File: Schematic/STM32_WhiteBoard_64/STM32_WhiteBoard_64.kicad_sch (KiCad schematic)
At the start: 59 parts, among them J1 SWDIO+Serial, J2 USB_B_Micro, J3 Header2, J4 Header1, Q1 BC847BS, Q1 Si3493DDV, Q2 BC857BS, SW1 Boot0, SW2 Reset, SW3 User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

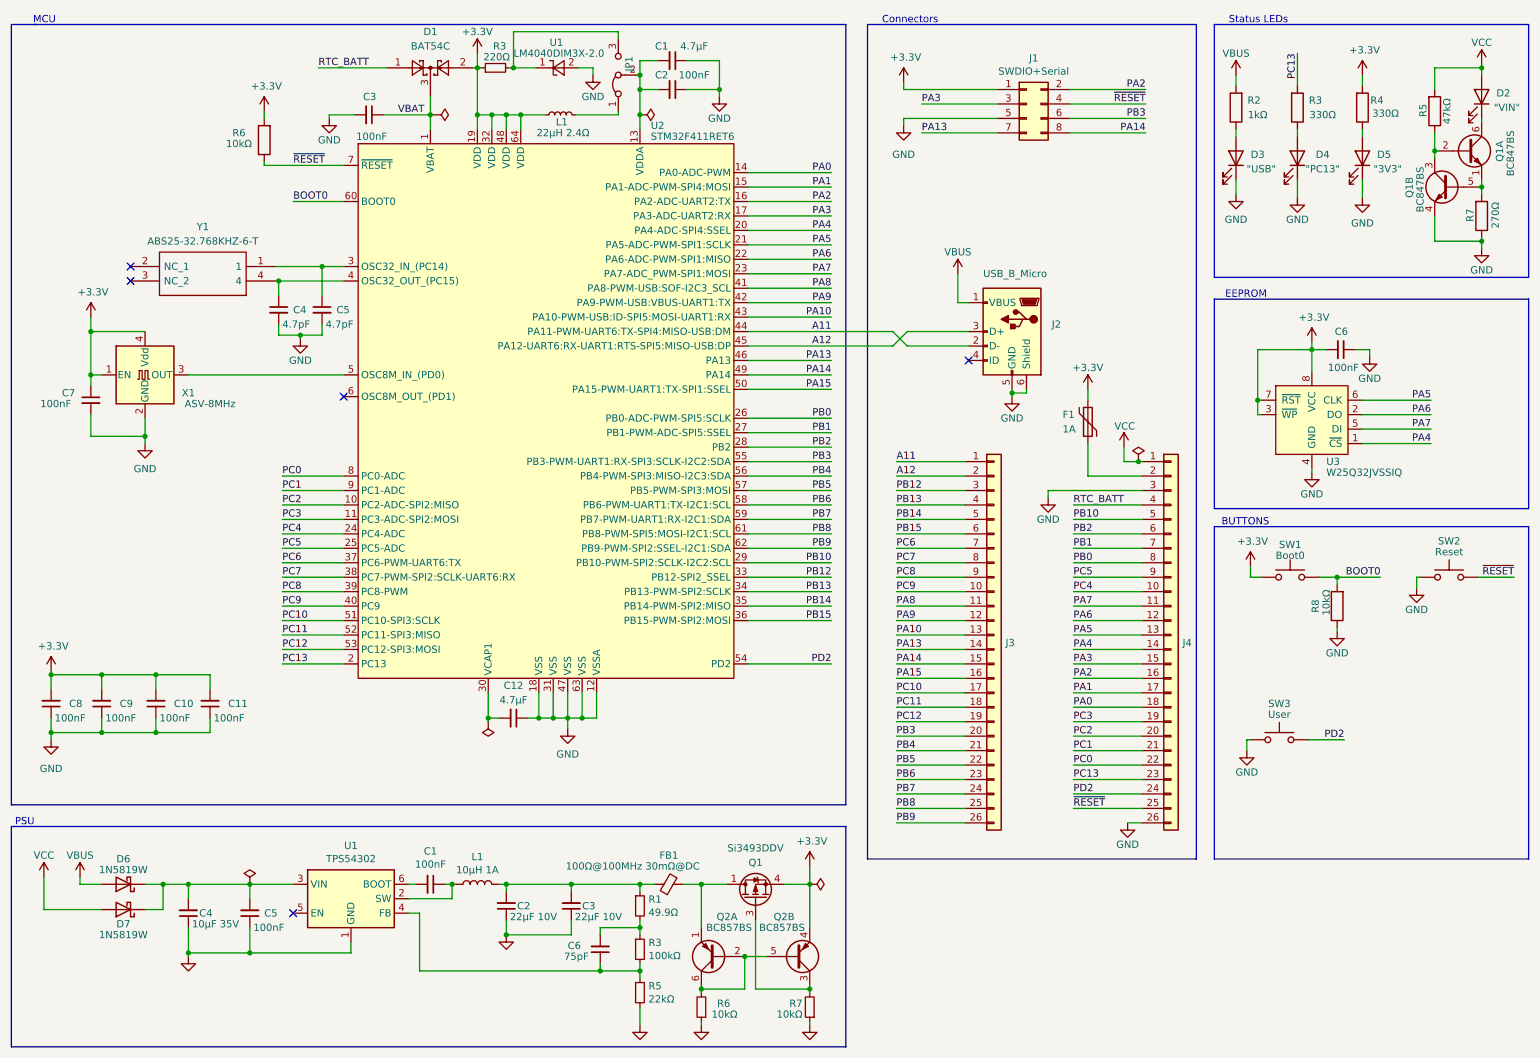
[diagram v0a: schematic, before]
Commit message: Added ESD protection for USB.
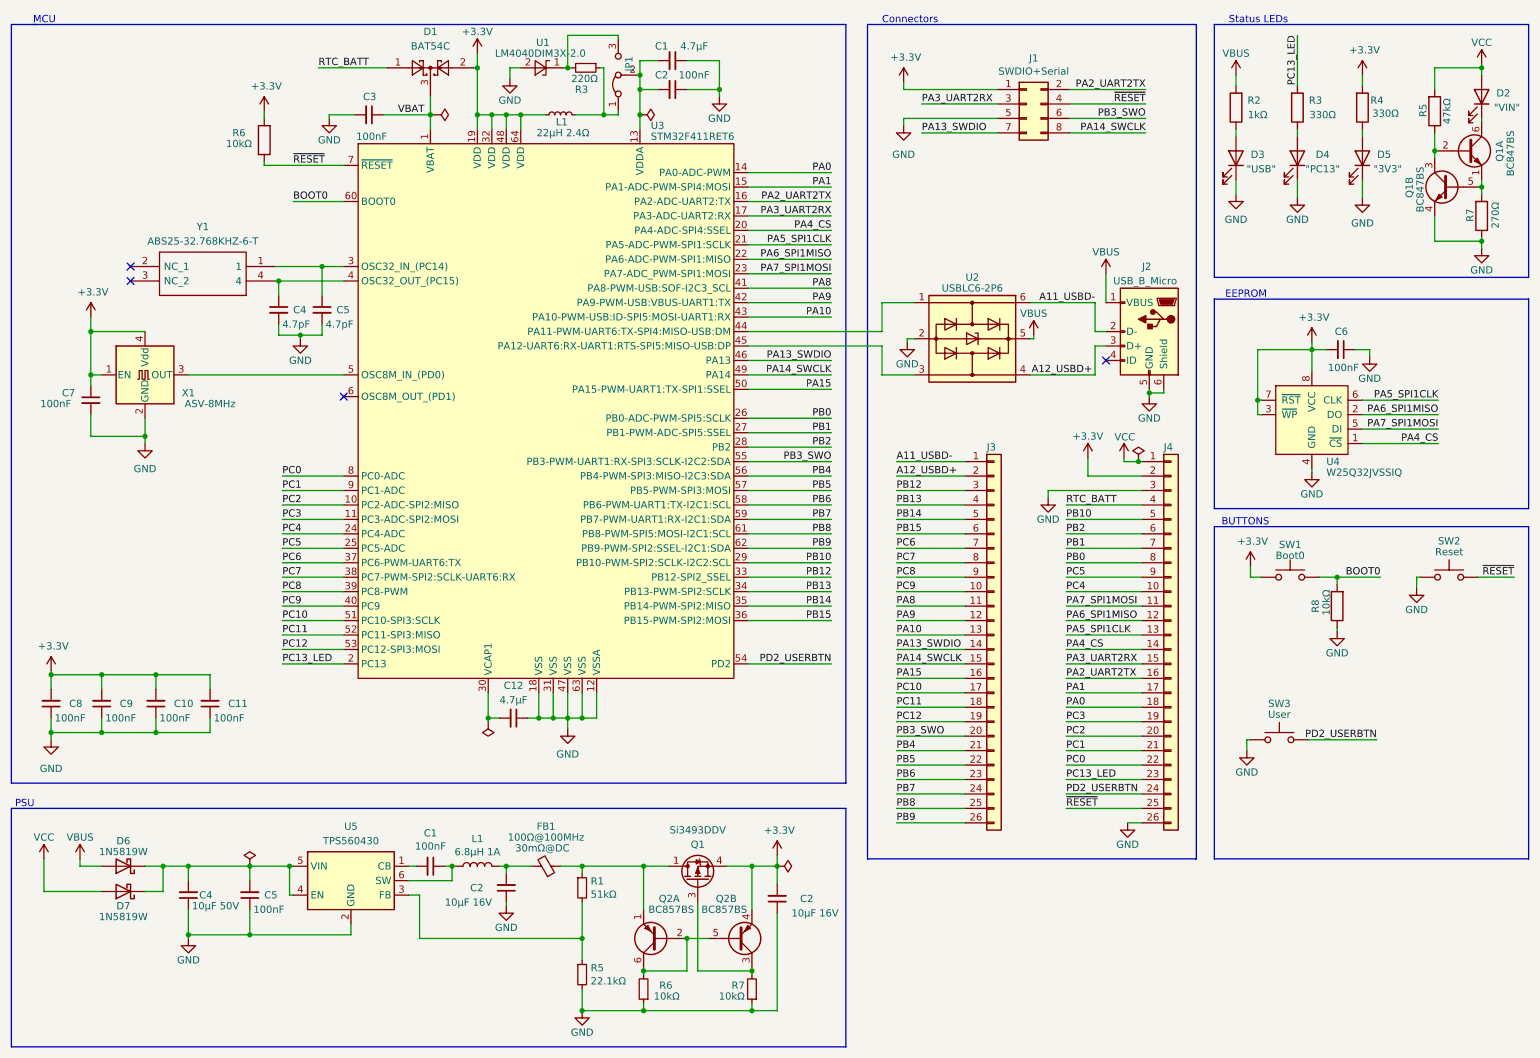
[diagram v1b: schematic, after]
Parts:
- removed C3: 22µF 10V, Capacitor_SMD:C_0603_1608Metric_Pad1.08x0.95mm_HandSolder, symbol Device:C_Small
- removed C6: 75pF, Capacitor_SMD:C_0603_1608Metric_Pad1.08x0.95mm_HandSolder, symbol Device:C_Small
- removed F1: 1A, Fuse:Fuse_1206_3216Metric_Pad1.42x1.75mm_HandSolder, symbol Device:Polyfuse
- removed J2: USB_B_Micro, digikey-footprints:USB_Micro_B_Female_10118194-0001LF, symbol Connector:USB_B_Micro
- removed R3: 100kΩ, Resistor_SMD:R_0603_1608Metric_Pad0.98x0.95mm_HandSolder, symbol Device:R_Small
- removed U1: TPS54302, Package_TO_SOT_SMD:SOT-23-6_Handsoldering, symbol Regulator_Switching:TPS54302
- added C2: 10µF 16V, Capacitor_SMD:C_0603_1608Metric_Pad1.08x0.95mm_HandSolder, symbol Device:C_Small
- added J2: USB_B_Micro, Retronics_Connectors:USB_Micro_B_Female_10118194-0001LF, symbol Retronics_Connectors:USB_B_Micro
- added U2: USBLC6-2P6, Retronics_IC:USBLC6-2SC6, symbol Retronics_Integrated_Circuits:USBLC6-2P6
- added U5: TPS560430, Package_TO_SOT_SMD:SOT-23-6, symbol Retronics_IC_Power:TPS560430
- C2: value 22µF 10V -> 10µF 16V
- C4: value 10µF 35V -> 10µF 50V; footprint Capacitor_SMD:C_0603_1608Metric_Pad1.08x0.95mm_HandSolder -> Capacitor_SMD:C_0805_2012Metric_Pad1.18x1.45mm_HandSolder
- FB1: value 100Ω@100MHz 30mΩ@DC -> 100Ω@100MHz; Comments (none) -> 30mΩ@DC
- L1: value 10µH 1A -> 6.8µH 1A; footprint Inductor_SMD:L_Taiyo-Yuden_NR-20xx_HandSoldering -> Inductor_SMD:L_1008_2520Metric_Pad1.43x2.20mm_HandSolder
- R1: value 49.9Ω -> 51kΩ
- R5: value 22kΩ -> 22.1kΩ
- SW1, SW2, SW3: footprint myDevices:PTS840ESDGMSMTRLFS -> Retronics_Switches:SKTHACE010
- renumbered U2 to U3, U3 to U4
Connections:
- net +3.3V: now also J4.2 (Pin_2), SW1.1, C2.2; no longer R3.1, SW1.2
- net BOOT0: now also SW1.2; no longer SW1.1
- net GND: now also C2.1, J2.5 (GND), J2.6 (Shield), U2.2 (GND), U5.2 (GND)
- net VBUS: now also J2.1 (VBUS), U2.5 (VBUS)
- net at JP1.1 (A), L1.2: now also R3.1
- net at R5.1: now also R1.2, U5.3 (FB)
- net at C1.1, L1.1: now also U5.6 (SW)
- net at C1.2: now also U5.1 (CB)
- net at C4.2, C5.2, D6.1 (K)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: now also U5.4 (EN), U5.5 (VIN)
- net at FB1.1, R1.1: now also Q1.1 (D), Q1.2 (D), Q1.5 (D), Q1.6 (D), Q2.1 (E1); no longer C2.2, L1.2
- net A11: no longer names the net of U3.44 (PA11-PWM-UART6:TX-SPI4:MISO-USB:DM)
- net A11: now also U2.1 (I/O1); no longer J3.1 (Pin_1)
- net A12: no longer names the net of U3.45 (PA12-UART6:RX-UART1:RTS-SPI5:MISO-USB:DP)
- net A12: now also U2.3 (I/O2); no longer J3.2 (Pin_2)
- net PA13 renamed PA13_SWDIO
- net PA14 renamed PA14_SWCLK
- net PA2 renamed PA2_UART2TX
- net PA3 renamed PA3_UART2RX
- net PA4 renamed PA4_CS
- net PA5 renamed PA5_SPI1CLK
- net PA6 renamed PA6_SPI1MISO
- net PA7 renamed PA7_SPI1MOSI
- net PB3 renamed PB3_SWO
- net PC13 renamed PC13_LED
- net PD2 renamed PD2_USERBTN
- new net: C2.2, FB1.2, L1.2
- new net A11_USBD-: J2.2 (D-), J3.1 (Pin_1), U2.6 (I/O1)
- new net A12_USBD+: J2.3 (D+), J3.2 (Pin_2), U2.4 (I/O2)
- no-connect marks 5 -> 4
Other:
- moved on the sheet: C1, C2, C4, C5, D6, D7, FB1, L1, Q1, Q2A, Q2B, R1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
